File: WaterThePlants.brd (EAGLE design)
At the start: 31.8 x 19.1 mm, 7 parts, among them U1 TINY45

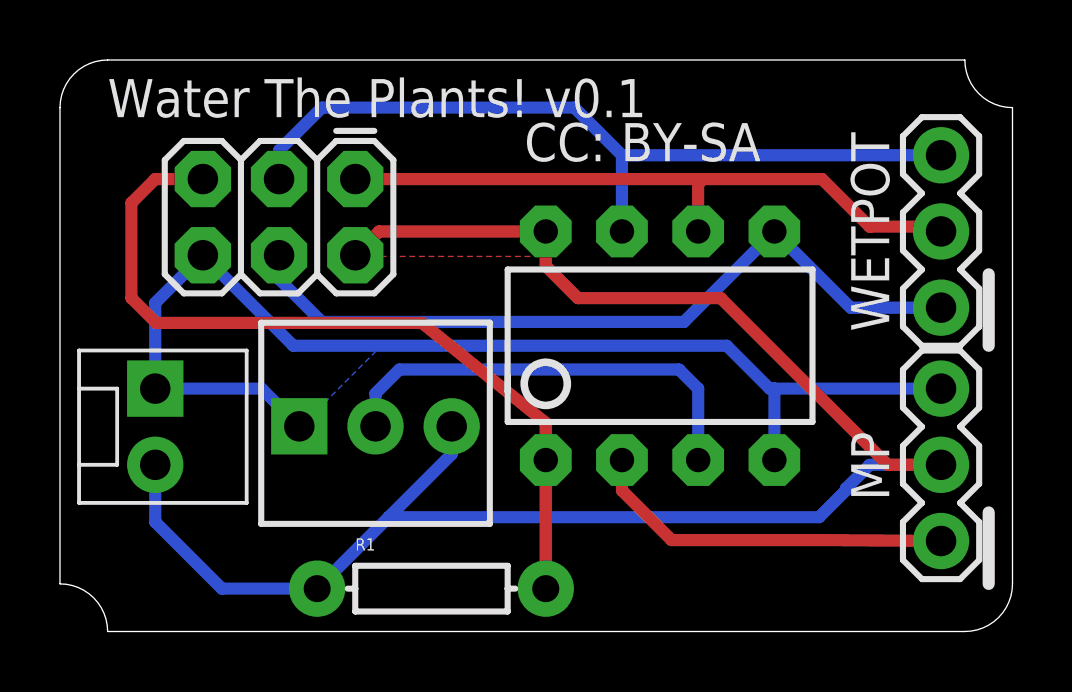
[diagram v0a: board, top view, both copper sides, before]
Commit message: Fixed so wetpot is reading on an analog pin. Updated to v0.2
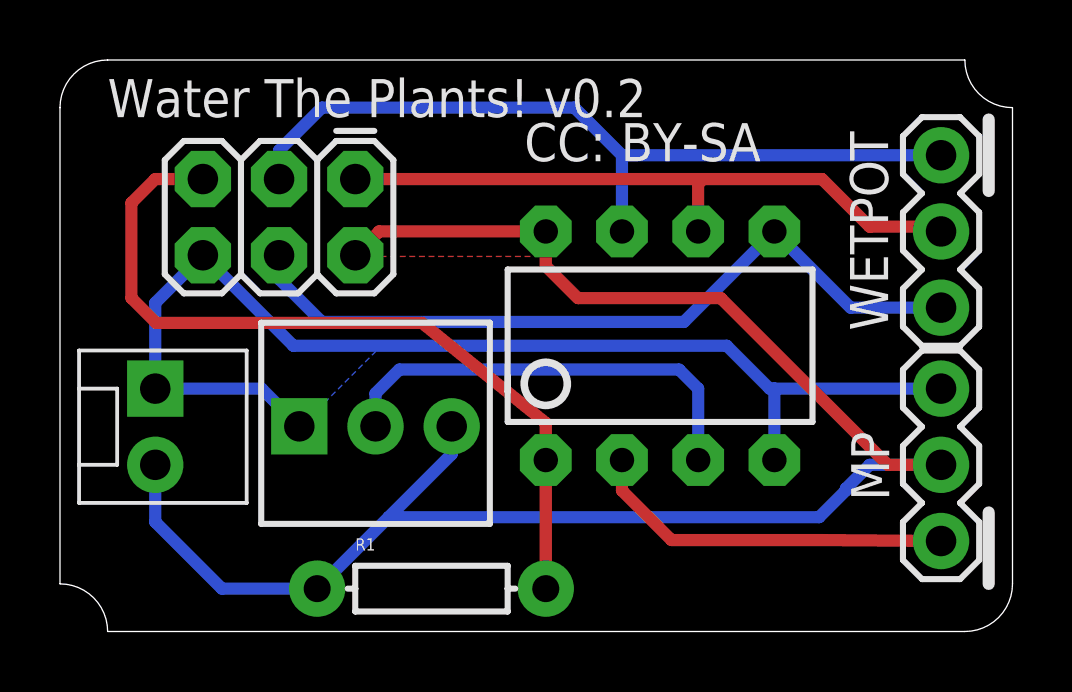
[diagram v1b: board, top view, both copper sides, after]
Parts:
- moved WETPOT 5.08 mm to (29.4, 10.8), turned to 90 degrees
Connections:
- net DIGITAL2: now also JP1.4, U1.5; no longer JP1.3, U1.7
- net WETSIG: now also JP1.3, U1.7; no longer JP1.4, U1.5
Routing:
- net WETSIG: track 25.8 -> 26.8 mm
- net DIGITAL2: track 26.8 -> 25.8 mm
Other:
- board text added: "Water The Plants! v0.2"
- board text removed: "Water The Plants! v0.1"
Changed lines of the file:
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@@
 <grid distance="0.0078125" unitdist="inch" unit="inch" style="lines" multiple="1" display="yes" altdistance="0.025" altunitdist="inch" altunit="inch"/>
 <layers>
-<layer number="1" name="Top" color="4" fill="1" visible="yes" active="yes"/>
-<layer number="16" name="Bottom" color="1" fill="1" visible="yes" active="yes"/>
+<layer number="1" name="Top" color="4" fill="1" visible="no" active="yes"/>
+<layer number="16" name="Bottom" color="1" fill="1" visible="no" active="yes"/>
 <layer number="17" name="Pads" color="2" fill="1" visible="yes" active="yes"/>
 <layer number="18" name="Vias" color="2" fill="1" visible="yes" active="yes"/>
@@
 <layer number="118" name="Rect_Pads" color="7" fill="1" visible="no" active="no"/>
 <layer number="121" name="_tsilk" color="7" fill="1" visible="yes" active="yes"/>
-<layer number="122" name="_bsilk" color="7" fill="1" visible="yes" active="yes"/>
+<layer number="122" name="_bsilk" color="7" fill="1" visible="no" active="yes"/>
 <layer number="123" name="tTestmark" color="7" fill="1" visible="yes" active="yes"/>
 <layer number="124" name="bTestmark" color="7" fill="1" visible="yes" active="yes"/>
@@
 <wire x1="30.95625" y1="1.5875" x2="30.95625" y2="3.96875" width="0.4064" layer="121"/>
 <wire x1="0" y1="1.5875" x2="1.5875" y2="0" width="0" layer="20" curve="-90"/>
-<wire x1="30.95625" y1="9.525" x2="30.95625" y2="11.90625" width="0.4064" layer="121"/>
+<wire x1="30.95625" y1="14.684375" x2="30.95625" y2="17.065625" width="0.4064" layer="121"/>
 <wire x1="30.1625" y1="19.05" x2="31.75" y2="17.4625" width="0" layer="20" curve="90"/>
 <wire x1="30.1625" y1="0" x2="31.75" y2="1.5875" width="0" layer="20" curve="90"/>
-<text x="1.5875" y="17.145" size="1.27" layer="121" font="fixed">Water The Plants! v0.1</text>
+<text x="1.5875" y="17.145" size="1.27" layer="121" font="fixed">Water The Plants! v0.2</text>
 <text x="1.5875" y="17.145" size="1.27" layer="122" font="fixed" rot="MR0" align="bottom-right">andrewparnell.com</text>
 <text x="15.478125" y="15.6765625" size="1.27" layer="121" font="fixed">CC: BY-SA</text>
@@
 <attribute name="VALUE" x="16.8275" y="8.89" size="1.27" layer="27" ratio="10"/>
 </element>
-<element name="WETPOT" library="SparkFun-Connectors" package="1X03" value="" x="29.36875" y="15.875" smashed="yes" rot="R270">
-<attribute name="NAME" x="26.37155" y="13.319125" size="1.27" layer="25" font="fixed" ratio="10" rot="R270" align="bottom-center"/>
-<attribute name="VALUE" x="26.19375" y="17.145" size="1.27" layer="27" rot="R270"/>
+<element name="WETPOT" library="SparkFun-Connectors" package="1X03" value="" x="29.36875" y="10.795" smashed="yes" rot="R90">
+<attribute name="NAME" x="27.60345" y="13.350875" size="1.27" layer="25" font="fixed" ratio="10" rot="R90" align="bottom-center"/>
+<attribute name="VALUE" x="32.54375" y="9.525" size="1.27" layer="27" rot="R90"/>
 </element>
 <element name="JP1" library="SparkFun-Connectors" package="2X3" value="AVR_SPI_PRG_6PTH" x="9.8425" y="15.08125" smashed="yes" rot="R180"/>
@@
 </polygon>
 </signal>
-<signal name="WETSIG">
+<signal name="DIGITAL2">
 <contactref element="JP1" pad="4"/>
-<contactref element="WETPOT" pad="3"/>
 <contactref element="U1" pad="5"/>
 <wire x1="7.3025" y1="12.54125" x2="7.3025" y2="11.7475" width="0.4064" layer="16"/>
@@
 <wire x1="20.79625" y1="10.31875" x2="23.8125" y2="13.335" width="0.4064" layer="16"/>
 <wire x1="26.3525" y1="10.795" x2="23.8125" y2="13.335" width="0.4064" layer="16"/>
+<contactref element="WETPOT" pad="1"/>
 <wire x1="29.36875" y1="10.795" x2="26.3525" y2="10.795" width="0.4064" layer="16"/>
 </signal>
@@
 <wire x1="29.21" y1="13.49375" x2="29.36875" y2="13.335" width="0.4064" layer="1"/>
 </signal>
-<signal name="DIGITAL2">
-<contactref element="WETPOT" pad="1"/>
+<signal name="WETSIG">
 <contactref element="U1" pad="7"/>
 <contactref element="JP1" pad="3"/>
 <wire x1="18.7325" y1="13.335" x2="18.7325" y2="15.875" width="0.4064" layer="16"/>
-<wire x1="29.36875" y1="15.875" x2="18.7325" y2="15.875" width="0.4064" layer="16"/>
 <wire x1="18.7325" y1="15.875" x2="17.145" y2="17.4625" width="0.4064" layer="16"/>
 <wire x1="17.145" y1="17.4625" x2="8.73125" y2="17.4625" width="0.4064" layer="16"/>
 <wire x1="8.73125" y1="17.4625" x2="7.3025" y2="16.03375" width="0.4064" layer="16"/>
 <wire x1="7.3025" y1="16.03375" x2="7.3025" y2="15.08125" width="0.4064" layer="16"/>
+<contactref element="WETPOT" pad="3"/>
+<wire x1="29.36875" y1="15.875" x2="18.7325" y2="15.875" width="0.4064" layer="16"/>
 </signal>
 <signal name="N$6">
